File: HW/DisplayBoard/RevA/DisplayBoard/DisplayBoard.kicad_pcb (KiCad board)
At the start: 2 copper layers, 13 parts, among them J1 Conn_02x06_Odd_Even, SW1 Rotary_Encoder_Switch, U1 Tactile_Switch_SPST-NO, U2 Tactile_Switch_SPST-NO, U3 Tactile_Switch_SPST-NO, U4 Tactile_Switch_SPST-NO

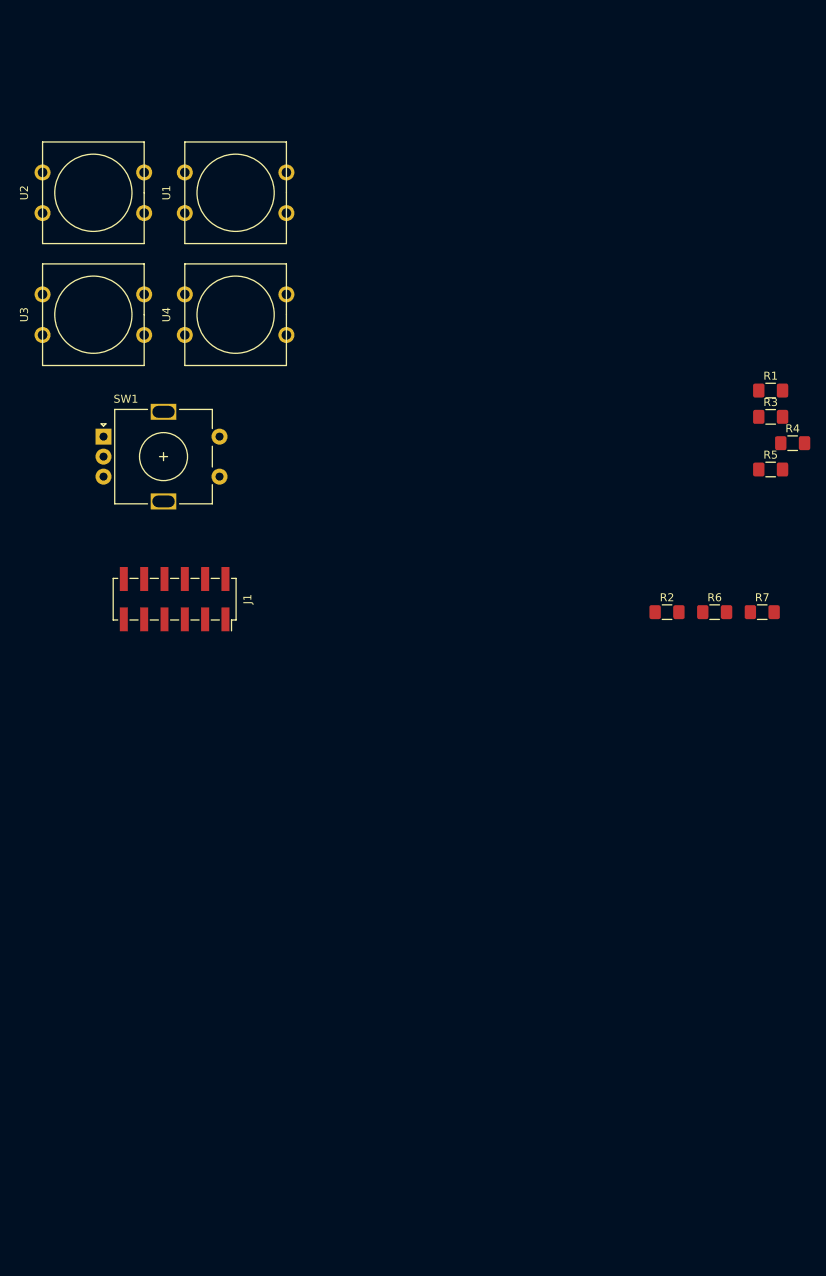
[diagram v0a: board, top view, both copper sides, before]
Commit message: updated front panel board layouts
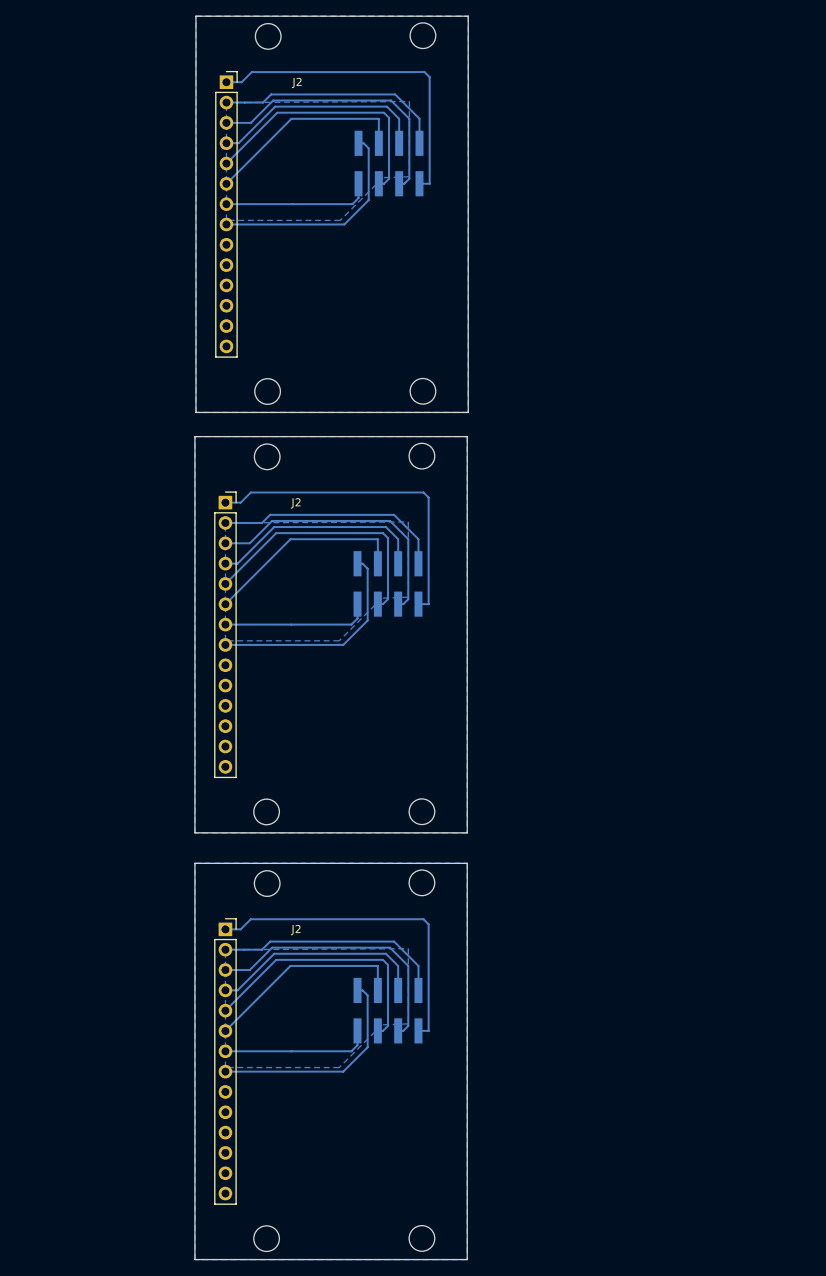
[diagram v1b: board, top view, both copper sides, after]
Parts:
- removed the J1 at (104.1, 99.1)
- removed R1, R2, R3, R4: 220R, Resistor_SMD:R_1206_3216Metric_Pad1.42x1.75mm_HandSolder
- removed R5, R6, R7: 10K, Resistor_SMD:R_1206_3216Metric_Pad1.42x1.75mm_HandSolder
- removed SW1: Rotary_Encoder_Switch, Rotary_Encoder:RotaryEncoder_Alps_EC11E-Switch_Vertical_H20mm
- removed U1, U2, U3, U4: Tactile_Switch_SPST-NO, 12x12x7_3mmTactilePushButtonMomentary:12x12x7_3mmTactilePushButtonMomentary
- added J1: Conn_02x04_Odd_Even, Connector_PinHeader_2.54mm:PinHeader_2x04_P2.54mm_Vertical_SMD, B.Cu at (130.8, 150.5)
- added J1: Conn_02x04_Odd_Even, Connector_PinHeader_2.54mm:PinHeader_2x04_P2.54mm_Vertical_SMD, B.Cu at (130.8, 97.2)
- added J1: Conn_02x04_Odd_Even, Connector_PinHeader_2.54mm:PinHeader_2x04_P2.54mm_Vertical_SMD, B.Cu at (130.9, 44.6)
- added J2: Conn_01x14, Connector_PinSocket_2.54mm:PinSocket_1x14_P2.54mm_Vertical, F.Cu at (110.5, 140.3)
- added J2: Conn_01x14, Connector_PinSocket_2.54mm:PinSocket_1x14_P2.54mm_Vertical, F.Cu at (110.5, 87.0)
- added J2: Conn_01x14, Connector_PinSocket_2.54mm:PinSocket_1x14_P2.54mm_Vertical, F.Cu at (110.6, 34.4)
- added REF**: MountingHole_3.2mm_M3, MountingHole:MountingHole_3.2mm_M3, F.Cu at (115.6, 179.0)
- added REF**: MountingHole_3.2mm_M3, MountingHole:MountingHole_3.2mm_M3, F.Cu at (135.2, 73.1)
- added REF**: MountingHole_3.2mm_M3, MountingHole:MountingHole_3.2mm_M3, F.Cu at (115.8, 28.7)
- added REF**: MountingHole_3.2mm_M3, MountingHole:MountingHole_3.2mm_M3, F.Cu at (115.8, 73.1)
- added REF**: MountingHole_3.2mm_M3, MountingHole:MountingHole_3.2mm_M3, F.Cu at (115.7, 134.6)
- added REF**: MountingHole_3.2mm_M3, MountingHole:MountingHole_3.2mm_M3, F.Cu at (135.1, 134.5)
- added REF**: MountingHole_3.2mm_M3, MountingHole:MountingHole_3.2mm_M3, F.Cu at (135.1, 179.0)
- added REF**: MountingHole_3.2mm_M3, MountingHole:MountingHole_3.2mm_M3, F.Cu at (115.6, 125.7)
- added REF**: MountingHole_3.2mm_M3, MountingHole:MountingHole_3.2mm_M3, F.Cu at (115.7, 81.3)
- added REF**: MountingHole_3.2mm_M3, MountingHole:MountingHole_3.2mm_M3, F.Cu at (135.1, 81.2)
- added REF**: MountingHole_3.2mm_M3, MountingHole:MountingHole_3.2mm_M3, F.Cu at (135.1, 125.6)
- added REF**: MountingHole_3.2mm_M3, MountingHole:MountingHole_3.2mm_M3, F.Cu at (135.2, 28.6)
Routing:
- net (no net): track 0.00 -> 468.7 mm
- net /Display/TFT_VCC: track 0.00 -> 40.8 mm
- net /Display/TFT_CS: track 0.00 -> 34.0 mm
- net /Display/TFT_DC: track 0.00 -> 32.4 mm
- net /Display/TFT_GND: track 0.00 -> 28.9 mm
- net /Display/TFT_RST: track 0.00 -> 27.2 mm
- net /Display/TFT_LED: track 0.00 -> 27.0 mm
- net /Display/TFT_MOSI: track 0.00 -> 25.5 mm
- net /Display/TFT_SCK: track 0.00 -> 18.6 mm
- added copper zone on B.Cu, net (none)
- added copper zone on B.Cu, net /Display/TFT_VCC
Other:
- board outline added: 34.2 x 155.4 mm
- board text added: "Print Layers: - B.Cu - Dwgs.User Print options: "Exclude print edges" = True "Mirrored" = False"
- board text added: "VCC"
